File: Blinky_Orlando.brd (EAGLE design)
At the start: 38.1 x 38.1 mm, 15 parts, among them IC1 OP-DUALRM

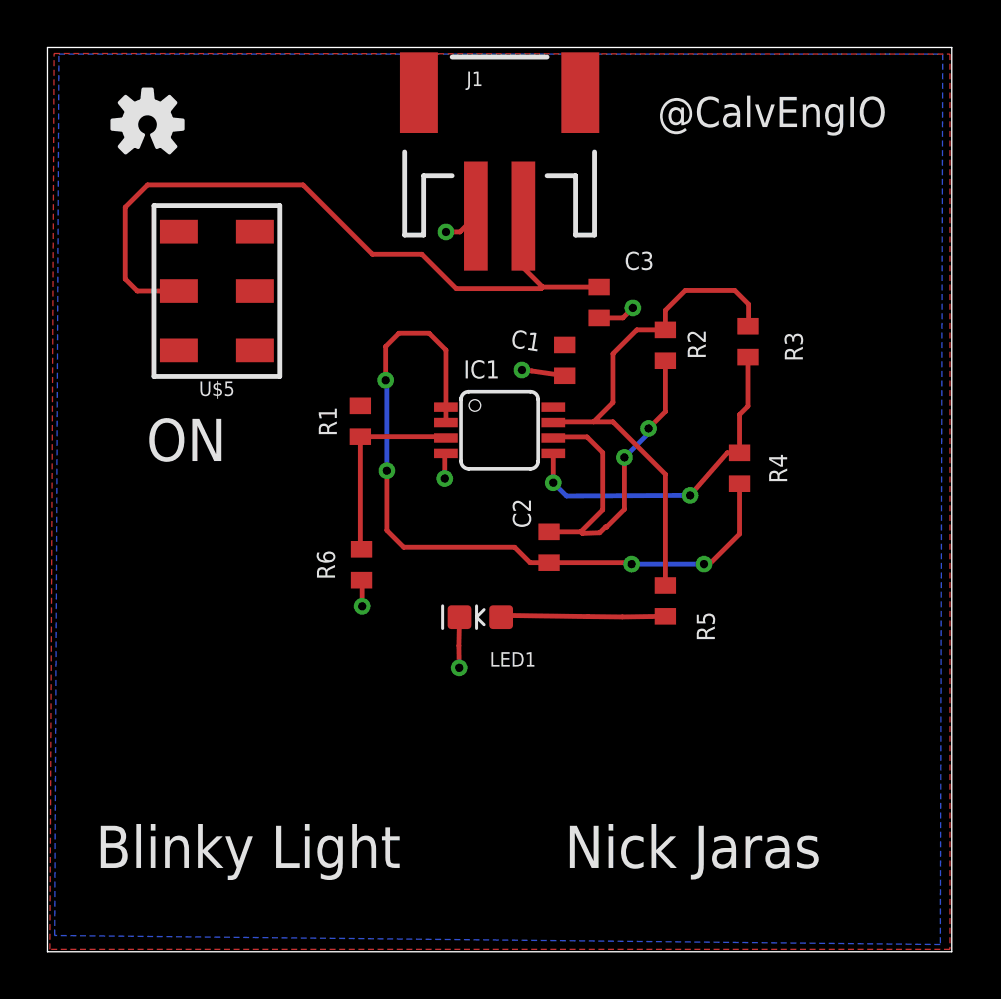
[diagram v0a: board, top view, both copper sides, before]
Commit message: made changes to Nick's board by moving the silkscreen of his name over just a test  and added my board as a reference
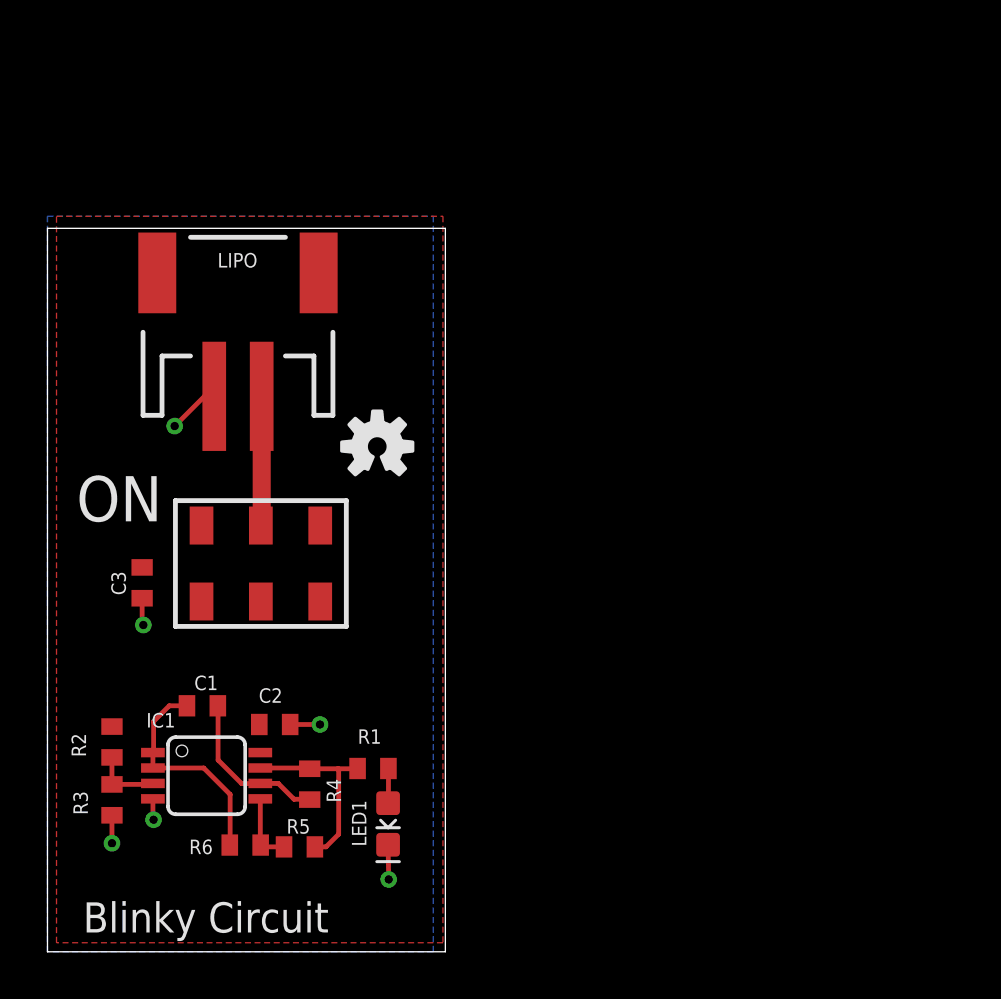
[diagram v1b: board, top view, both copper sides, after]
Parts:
- removed J1: (no value), CalvEngIO-Connectors:JST-2-SMD
- removed U$5: SWITCH.JS202011JCQN, CalvEngIO-Switches:SWITCH.00
- added LIPO: (no value), CalvEngIO-Connectors:JST-2-SMD
- added ON/OFF: SWITCH.JS202011JCQN, CalvEngIO-Switches:SWITCH.00
- C1, C2, C3: value 100 nF -> 100n
- R1: value 10k -> 309
- R2: value 3.3 M -> 10k
- R3: value 10k -> 10k
- R4: value 10k -> 3.3M
- R5: value 300 -> 10k
- moved R3 33.0 mm to (2.72, 6.40)
- moved U$4 31.6 mm to (8.86, 12.0), flipped to the bottom
- moved R2 28.7 mm to (2.72, 8.84)
- moved C3 22.6 mm to (3.99, 15.5)
- moved R4 22.5 mm to (11.0, 7.06), turned to 270 degrees
- moved C1 21.1 mm to (6.53, 10.4), turned to 180 degrees
- moved IC1 19.1 mm to (6.71, 7.42)
- moved R5 18.6 mm to (10.6, 4.42), turned to 180 degrees
- moved LOGO1 16.7 mm to (13.9, 21.3)
- moved R1 14.6 mm to (13.7, 7.72), turned to 180 degrees
- moved C2 13.8 mm to (9.58, 9.58), turned to 180 degrees
- moved R6 12.8 mm to (8.33, 4.50), turned to 0 degrees
- moved LED1 9.54 mm to (14.4, 5.38), turned to 270 degrees
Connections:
- removed net N$10: IC1.3, R1.1, R6.2
- removed net N$8: C2.2, IC1.1, IC1.2, R4.1
- new net N$5: C1.2, IC1.1, IC1.2, R6.1
- new net N$6: IC1.3, R2.1, R3.2
- net GND: now also C2.1, LIPO.1, R3.1; no longer C1.2, J1.1, R6.1
- net N$1: now also C1.1, IC1.6, R4.2; no longer C3.1, J1.2, U$5.2
- net N$2: now also IC1.7, R1.2, R4.1, R5.1; no longer IC1.5, R3.1, R4.2
- net N$3: now also LIPO.2, ON/OFF.2; no longer IC1.7, R2.2, R3.2, R5.2
- net N$4: now also IC1.5, R5.2, R6.2; no longer C2.1, IC1.6, R2.1
- net N$7: now also R1.1; no longer R5.1
- net VLIPO: now also C2.2, C3.1, ON/OFF.1, R2.2; no longer C1.1, R1.2, U$5.1
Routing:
- net N$8: track 32.0 -> 0.00 mm, vias 4 -> 0
- net N$1: track 31.0 -> 6.85 mm
- net N$3: track 22.0 -> 5.46 mm
- net N$4: track 16.7 -> 2.97 mm, vias 2 -> 0
- net N$5: track 0.00 -> 9.51 mm
- net N$10: track 8.39 -> 0.00 mm
- net N$2: track 14.3 -> 8.11 mm, vias 2 -> 0
- net N$7: track 7.00 -> 1.47 mm
- net N$6: track 0.00 -> 2.88 mm
- net GND: track 9.28 -> 8.12 mm
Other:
- board size 38.1 x 38.1 mm -> 16.8 x 30.5 mm
- board text added: "Blinky Circuit"
- board text removed: "Blinky Light"
- board text removed: "Nick Jaras"
